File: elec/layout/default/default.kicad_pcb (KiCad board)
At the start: 4 copper layers, 45 x 167 mm, 141 parts

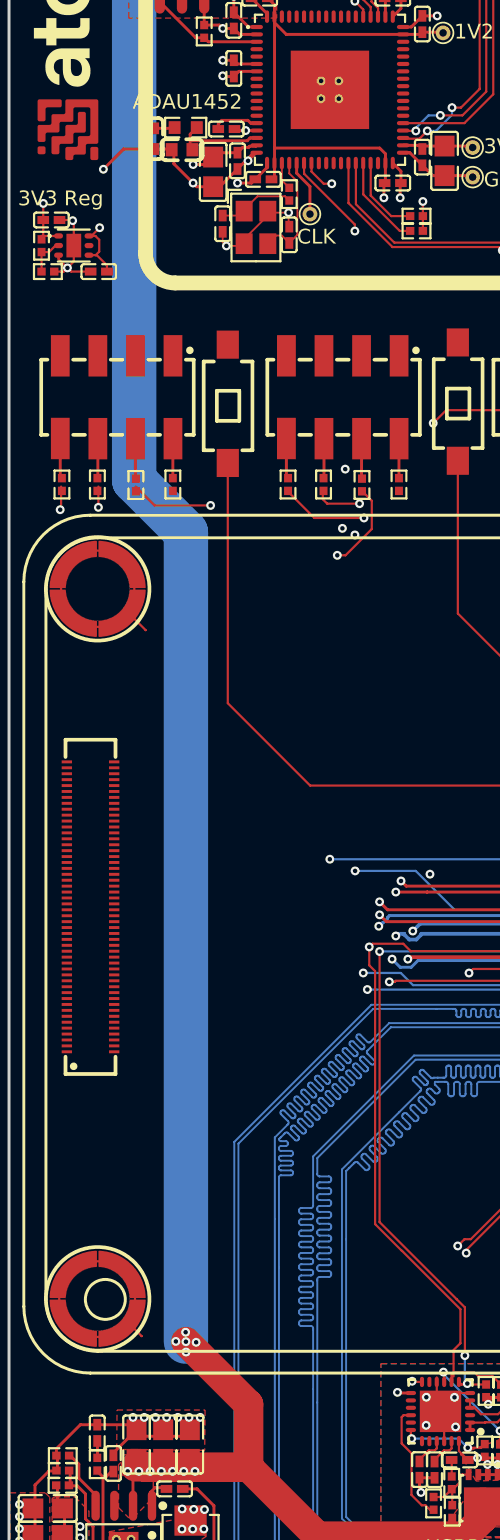
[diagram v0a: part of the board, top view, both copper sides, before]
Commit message: exclude PCB checks
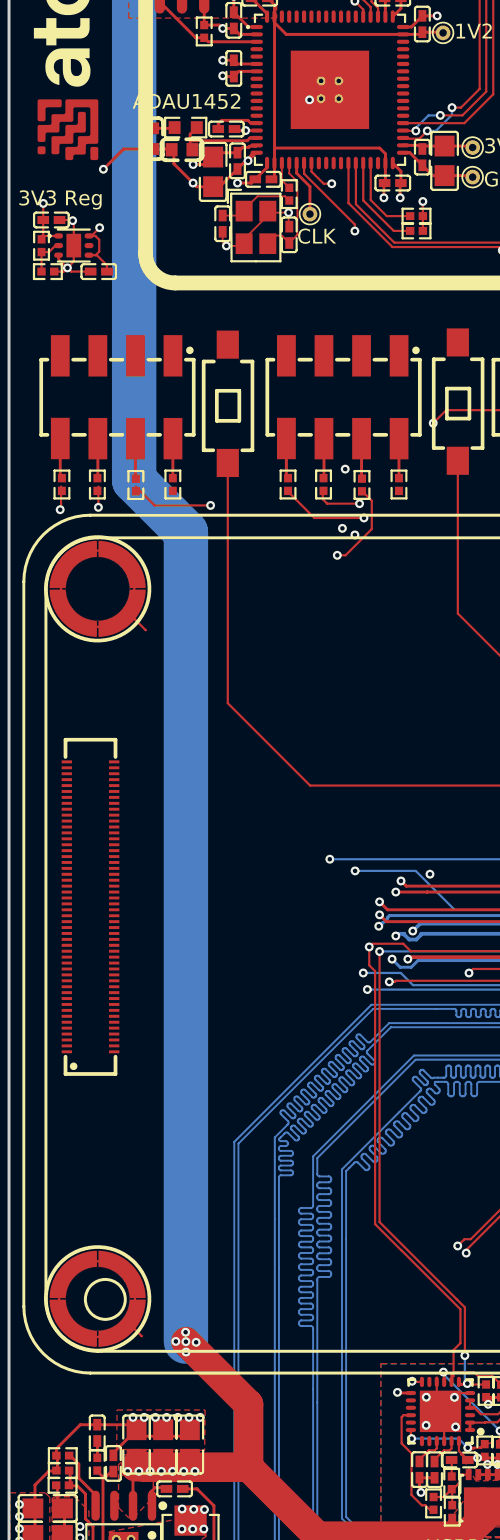
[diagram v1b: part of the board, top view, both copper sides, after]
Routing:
- net dsp-net: track 0.00 -> 3.60 mm
- net gnd: track 261.6 -> 263.3 mm, vias 61 -> 62
- added copper zone on F.Cu, net dsp-net

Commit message: update net names
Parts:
- R37: value 1.8kΩ ±1% 62.5mW -> 10kΩ ±1% 62.5mW; footprint YAGEO_RC0402FR_071K8L:R0402 -> UNI_ROYAL_0402WGF1002TCE:R0402
- R38: value 10kΩ ±1% 62.5mW -> 54.9kΩ ±1% 62.5mW; footprint UNI_ROYAL_0402WGF1002TCE:R0402 -> UNI_ROYAL_0402WGF5492TCE:R0402
